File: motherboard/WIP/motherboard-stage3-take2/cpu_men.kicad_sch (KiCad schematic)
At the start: 26 parts, among them J1 HALT, J2 Write Protect, U2 74HC245, U3 MC6809, U4 74HC245, U5 28C64, U6 74HC245, U7 AS6C4008, U8 AS6C4008, Y1 12MHz

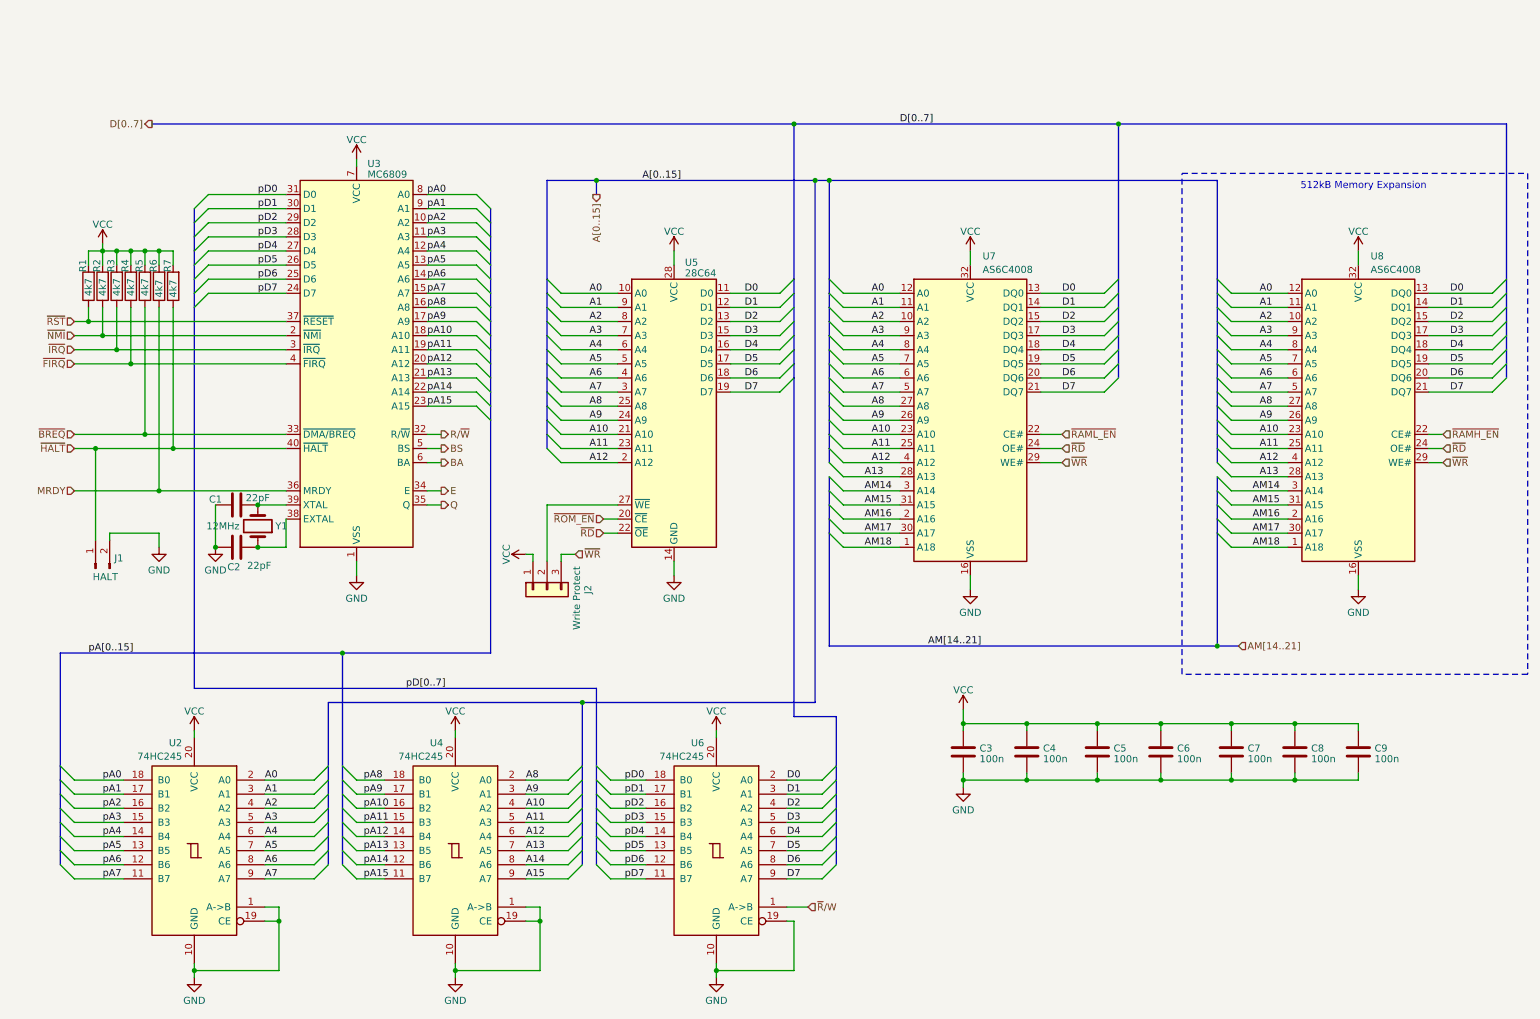
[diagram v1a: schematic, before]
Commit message: Updated stage 2 and stage 3, and started on a cf addon
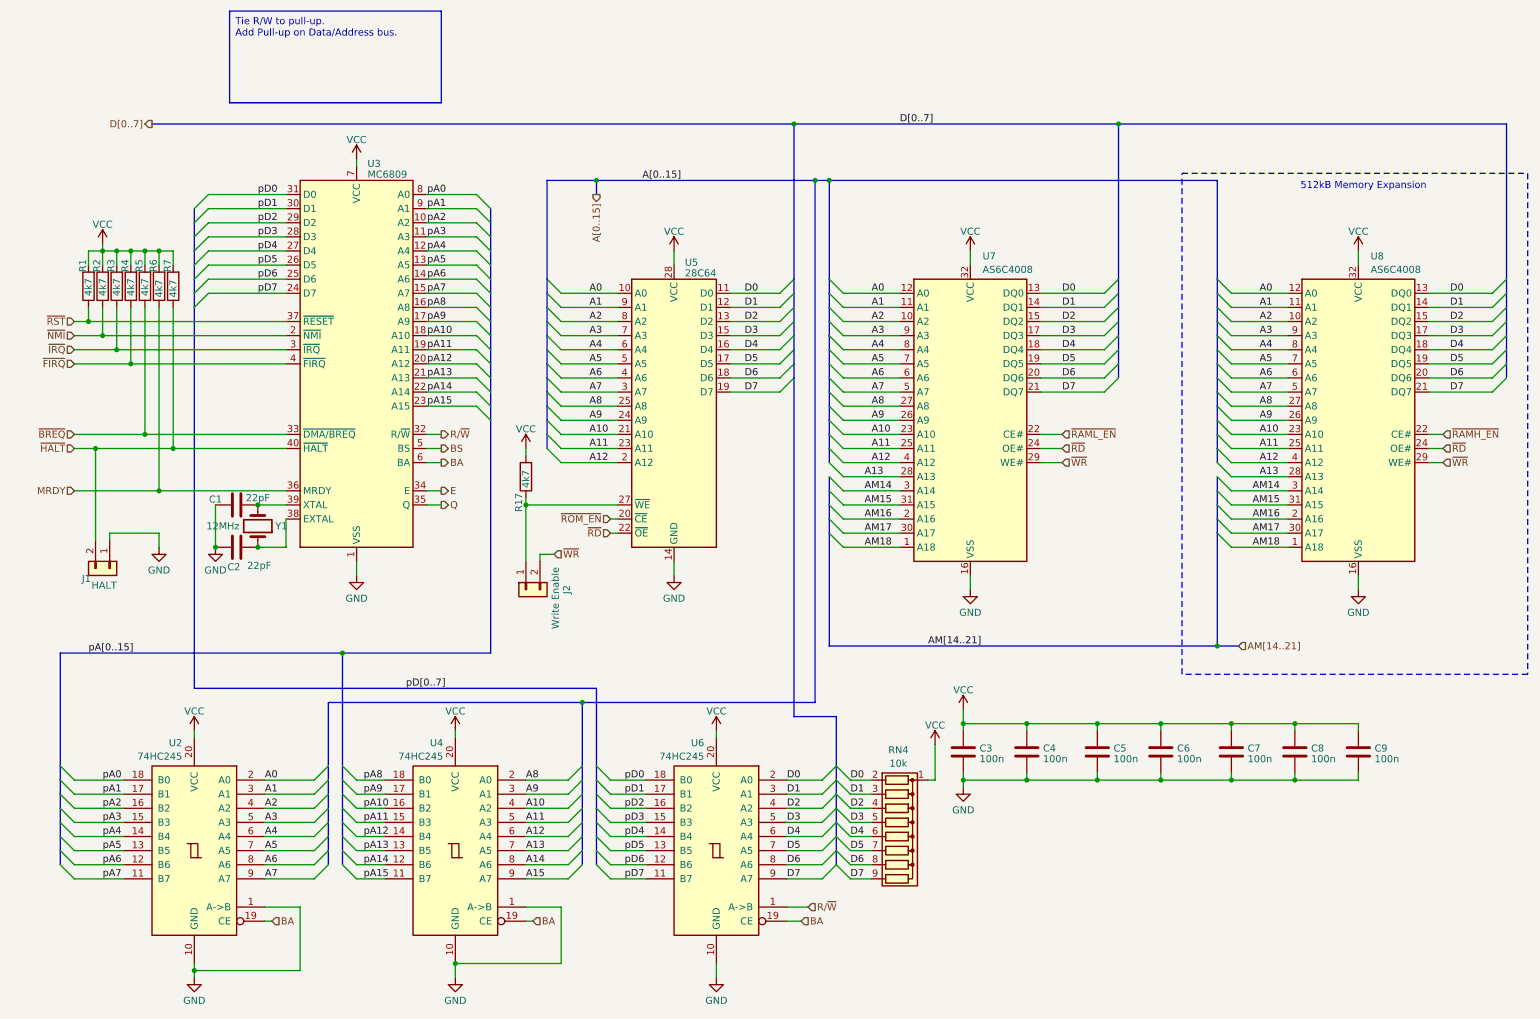
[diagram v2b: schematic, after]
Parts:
- added R17: 4k7, Resistor_THT:R_Axial_DIN0204_L3.6mm_D1.6mm_P7.62mm_Horizontal, symbol Device:R
- added RN4: 10k, Resistor_THT:R_Array_SIP9, symbol Device:R_Network08
- J1: symbol Connector:Conn_01x02_Male -> Connector_Generic:Conn_01x02
- J2: value Write Protect -> Write Enable; footprint Connector_PinHeader_2.54mm:PinHeader_1x03_P2.54mm_Vertical -> Connector_PinHeader_2.54mm:PinHeader_1x02_P2.54mm_Vertical; symbol Connector_Generic:Conn_01x03 -> Connector_Generic:Conn_01x02
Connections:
- net ~{R}/W is gone; now on net R/~{W}: U6.1 (A->B)
- net BA: now also U2.19 (CE), U4.19 (CE), U6.19 (CE)
- net D0: now also RN4.2 (R1)
- net D1: now also RN4.3 (R2)
- net D2: now also RN4.4 (R3)
- net D3: now also RN4.5 (R4)
- net D4: now also RN4.6 (R5)
- net D5: now also RN4.7 (R6)
- net D6: now also RN4.8 (R7)
- net D7: now also RN4.9 (R8)
- net GND: now also J1.1 (Pin_1); no longer J1.2 (Pin_2), U2.19 (CE), U4.19 (CE), U6.19 (CE)
- net VCC: now also R17.2, RN4.1 (common); no longer J2.1 (Pin_1)
- net ~{HALT}: now also J1.2 (Pin_2); no longer J1.1 (Pin_1)
- net ~{WR}: now also J2.2 (Pin_2); no longer J2.3 (Pin_3)
- net at U5.27 (~{WE}): now also J2.1 (Pin_1), R17.1; no longer J2.2 (Pin_2)
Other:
- company: (none) -> Eric Lind
- title: (none) -> MicroLind Processor & Memory

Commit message: Updates
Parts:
- R1, R17, R2, R3, R4, R5, R6, R7: value 4k7 -> 10k
